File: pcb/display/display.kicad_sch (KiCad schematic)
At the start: 18 parts, among them J1 Conn_01x08, U1 EA_DOGL128X-6

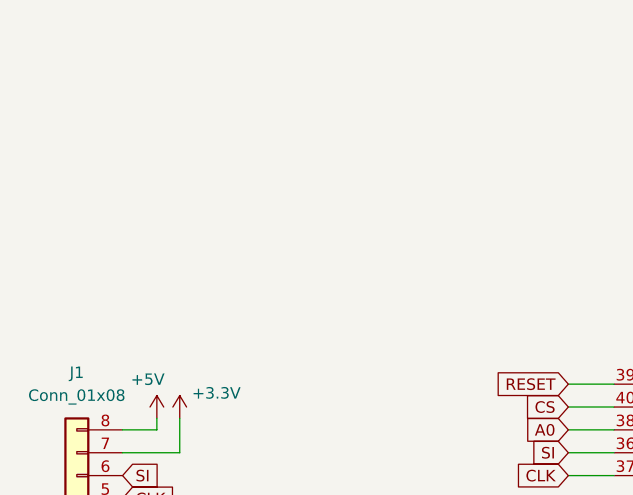
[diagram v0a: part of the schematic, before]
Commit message: resize display pcb to match main board
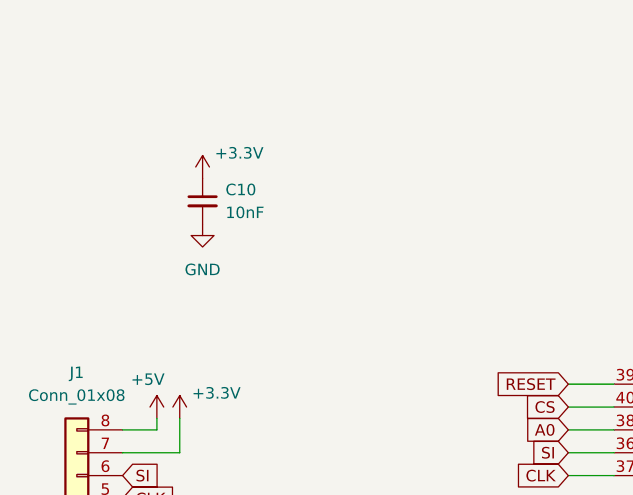
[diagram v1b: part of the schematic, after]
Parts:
- added C10: 10nF, Capacitor_THT:C_Disc_D3.8mm_W2.6mm_P2.50mm, symbol Device:C_Small
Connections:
- net +3.3V: now also C10.1
- net GND: now also C10.2
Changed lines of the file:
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@@
 (kicad_sch
-	(version 20231120)
+	(version 20250114)
 	(generator "eeschema")
-	(generator_version "8.0")
+	(generator_version "9.0")
 	(paper "A4")
 	(junction
@@
 	)
 	(symbol
+		(lib_id "Device:C_Small")
+		(at 48.26 40.64 0)
+		(unit 1)
+		(exclude_from_sim no)
+		(in_bom yes)
+		(on_board yes)
+		(dnp no)
+		(fields_autoplaced yes)
+		(property "Reference" "C10"
+			(at 50.8 39.3762 0)
+			(effects
+				(font
+					(size 1.27 1.27)
+				)
+				(justify left)
+			)
+		)
+		(property "Value" "10nF"
+			(at 50.8 41.9162 0)
+			(effects
+				(font
+					(size 1.27 1.27)
+				)
+				(justify left)
+			)
+		)
+		(property "Footprint" "Capacitor_THT:C_Disc_D3.8mm_W2.6mm_P2.50mm"
+			(at 48.26 40.64 0)
+			(effects
+				(font
+					(size 1.27 1.27)
+				)
+				(hide yes)
+			)
+		)
+		(property "Datasheet" "~"
+			(at 48.26 40.64 0)
+			(effects
+				(font
+					(size 1.27 1.27)
+				)
+				(hide yes)
+			)
+		)
+		(property "Description" "Unpolarized capacitor, small symbol"
+			(at 48.26 40.64 0)
+			(effects
+				(font
+					(size 1.27 1.27)
+				)
+				(hide yes)
+			)
+		)
+		(pin "2"
+		)
+		(pin "1"
+		)
+		(instances
+			(project ""
+				(path "/4189703f-2446-49af-a771-ea6ad1e86377"
+					(reference "C10")
+					(unit 1)
+				)
+			)
+		)
+	)
+	(symbol
 		(lib_id "power:GND")
 		(at 41.91 83.82 0)
@@
 	)
 	(symbol
+		(lib_id "power:+3.3V")
+		(at 48.26 38.1 0)
+		(unit 1)
+		(exclude_from_sim no)
+		(in_bom yes)
+		(on_board yes)
+		(dnp no)
+		(property "Reference" "#PWR013"
+			(at 48.26 41.91 0)
+			(effects
+				(font
+					(size 1.27 1.27)
+				)
+				(hide yes)
+			)
+		)
+		(property "Value" "+3.3V"
+			(at 52.324 35.306 0)
+			(effects
+				(font
+					(size 1.27 1.27)
+				)
+			)
+		)
+		(property "Footprint" ""
+			(at 48.26 38.1 0)
+			(effects
+				(font
+					(size 1.27 1.27)
+				)
+				(hide yes)
+			)
+		)
+		(property "Datasheet" ""
+			(at 48.26 38.1 0)
+			(effects
+				(font
+					(size 1.27 1.27)
+				)
+				(hide yes)
+			)
+		)
+		(property "Description" "Power symbol creates a global label with name \"+3.3V\""
+			(at 48.26 38.1 0)
+			(effects
+				(font
+					(size 1.27 1.27)
+				)
+				(hide yes)
+			)
+		)
+		(pin "1"
+		)
+		(instances
+			(project "display"
+				(path "/4189703f-2446-49af-a771-ea6ad1e86377"
+					(reference "#PWR013")
+					(unit 1)
+				)
+			)
+		)
+	)
+	(symbol
 		(lib_id "Device:C_Polarized_Small")
 		(at 78.74 82.55 180)
@@
 				(path "/4189703f-2446-49af-a771-ea6ad1e86377"
 					(reference "H1")
+					(unit 1)
+				)
+			)
+		)
+	)
+	(symbol
+		(lib_id "power:GND")
+		(at 48.26 43.18 0)
+		(unit 1)
+		(exclude_from_sim no)
+		(in_bom yes)
+		(on_board yes)
+		(dnp no)
+		(fields_autoplaced yes)
+		(property "Reference" "#PWR014"
+			(at 48.26 49.53 0)
+			(effects
+				(font
+					(size 1.27 1.27)
+				)
+				(hide yes)
+			)
+		)
+		(property "Value" "GND"
+			(at 48.26 48.26 0)
+			(effects
+				(font
+					(size 1.27 1.27)
+				)
+			)
+		)
+		(property "Footprint" ""
+			(at 48.26 43.18 0)
+			(effects
+				(font
+					(size 1.27 1.27)
+				)
+				(hide yes)
+			)
+		)
+		(property "Datasheet" ""
+			(at 48.26 43.18 0)
+			(effects
+				(font
+					(size 1.27 1.27)
+				)
+				(hide yes)
+			)
+		)
+		(property "Description" "Power symbol creates a global label with name \"GND\" , ground"
+			(at 48.26 43.18 0)
+			(effects
+				(font
+					(size 1.27 1.27)
+				)
+				(hide yes)
+			)
+		)
+		(pin "1"
+		)
+		(instances
+			(project "display"
+				(path "/4189703f-2446-49af-a771-ea6ad1e86377"
+					(reference "#PWR014")
 					(unit 1)
 				)
@@
 		)
 	)
+	(embedded_fonts no)
 )
